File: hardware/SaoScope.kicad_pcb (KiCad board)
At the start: 2 copper layers, 55 x 33 mm, 15 parts, among them J1 Conn_01x03_Pin, J2 Conn_01x04_Socket, SW1 TS-1077S-AR02016, SW2 TS-1077S-AR02016, SW3 TS-1077S-AR02016, SW4 TS-1077S-AR02016, U1 STM32G030F6Px, U2 LMC7660, U3 OPA197xDBV, U4 AP2120N-3.0TRG1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

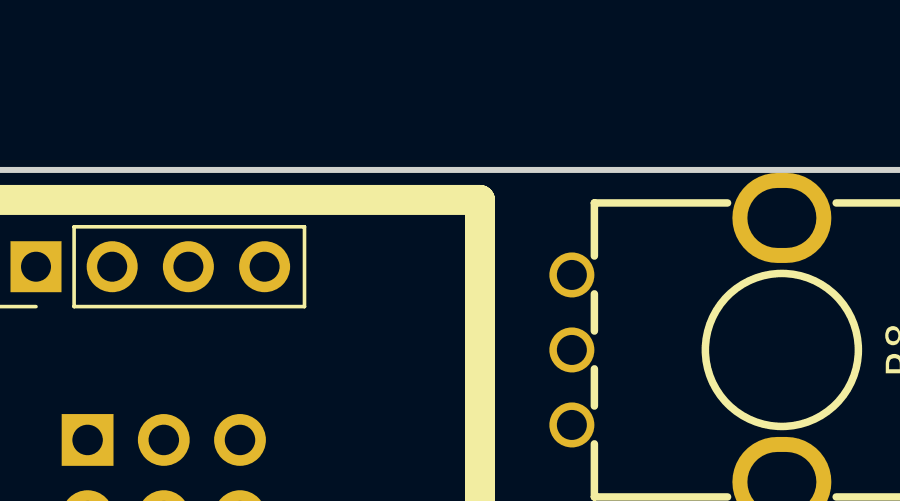
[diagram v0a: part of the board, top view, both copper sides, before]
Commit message: wire up pots and buttons, comments
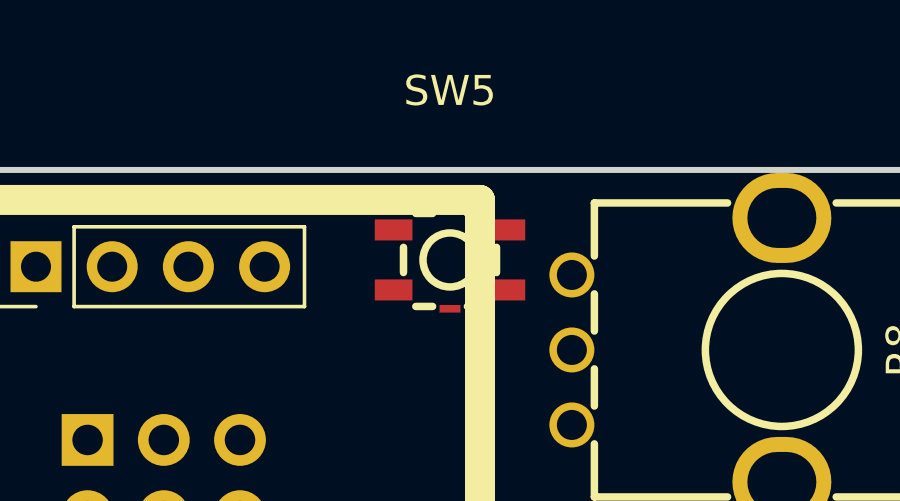
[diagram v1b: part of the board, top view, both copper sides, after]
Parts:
- added SW5: TS-1077S-AR02016, easyeda2kicad:KEY-SMD_4P-L3.1-W3.1-P2.00-LS4.0, F.Cu at (130.0, 64.0)
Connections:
- J2 pad 1: unconnected-(J2-Pin_1-Pad1) -> /I2C_SDA
- J2 pad 2: unconnected-(J2-Pin_2-Pad2) -> /I2C_SCL
- J2 pad 3: unconnected-(J2-Pin_3-Pad3) -> +3.3V
- J2 pad 4: unconnected-(J2-Pin_4-Pad4) -> GND
- R5 pad 1: unconnected-(R5-Pad1) -> Net-(R13-Pad2)
- R5 pad 2: unconnected-(R5-Pad2) -> /DIAL1
- R5 pad 3: unconnected-(R5-Pad3) -> Net-(R5-Pad3)
- R6 pad 1: unconnected-(R6-Pad1) -> Net-(R14-Pad2)
- R6 pad 2: unconnected-(R6-Pad2) -> /DIAL2
- R6 pad 3: unconnected-(R6-Pad3) -> Net-(R10-Pad1)
- R7 pad 1: unconnected-(R7-Pad1) -> Net-(R15-Pad2)
- R7 pad 2: unconnected-(R7-Pad2) -> /DIAL3
- R7 pad 3: unconnected-(R7-Pad3) -> Net-(R11-Pad1)
- R8 pad 1: unconnected-(R8-Pad1) -> Net-(R16-Pad2)
- R8 pad 2: unconnected-(R8-Pad2) -> /DIAL4
- R8 pad 3: unconnected-(R8-Pad3) -> Net-(R12-Pad1)
- SW1 pad 1: unconnected-(SW1-Pad1) -> /DIAL1
- SW1 pad 3: unconnected-(SW1-Pad3) -> GND
- SW1 pad 4: unconnected-(SW1-Pad4) -> GND
- SW2 pad 1: unconnected-(SW2-Pad1) -> /DIAL2
- SW2 pad 3: unconnected-(SW2-Pad3) -> GND
- SW2 pad 4: unconnected-(SW2-Pad4) -> GND
- SW3 pad 1: unconnected-(SW3-Pad1) -> /DIAL3
- SW3 pad 3: unconnected-(SW3-Pad3) -> GND
- SW3 pad 4: unconnected-(SW3-Pad4) -> GND
- SW4 pad 1: unconnected-(SW4-Pad1) -> /DIAL4
- SW4 pad 3: unconnected-(SW4-Pad3) -> GND
- SW4 pad 4: unconnected-(SW4-Pad4) -> GND
- U1 pad 1: unconnected-(U1-PB7/PB8-Pad1) -> /I2C1_SDA
- U1 pad 10: unconnected-(U1-PA3-Pad10) -> /DIAL3
- U1 pad 11: unconnected-(U1-PA4-Pad11) -> /PA4
- U1 pad 12: unconnected-(U1-PA5-Pad12) -> /I2S1_CK
- U1 pad 13: unconnected-(U1-PA6-Pad13) -> /DIAL4
- U1 pad 14: unconnected-(U1-PA7-Pad14) -> /I2S1_SD
- U1 pad 15: unconnected-(U1-PB0/PB1/PB2/PA8-Pad15) -> /I2S1_WS
- U1 pad 16: unconnected-(U1-PA11/PA9-Pad16) -> /PA11/PA9
- U1 pad 17: unconnected-(U1-PA12/PA10-Pad17) -> /PA12/PA10
- U1 pad 18: unconnected-(U1-PA13-Pad18) -> /SYS_SWDIO
- U1 pad 19: unconnected-(U1-PA14/PA15-Pad19) -> /SYS_SWCLK
- U1 pad 2: unconnected-(U1-PC14/PB9-Pad2) -> /RCC_OSC32_IN
- U1 pad 20: unconnected-(U1-PB3/PB4/PB5/PB6-Pad20) -> /I2C_SCL
- U1 pad 3: unconnected-(U1-PC15-Pad3) -> /RCC_OSC32_OUT
- U1 pad 4: unconnected-(U1-VDD-Pad4) -> +3V0
- U1 pad 5: unconnected-(U1-VSS-Pad5) -> GND
- U1 pad 6: unconnected-(U1-NRST-Pad6) -> /NRST
- U1 pad 7: unconnected-(U1-PA0-Pad7) -> /DIAL1
- U1 pad 8: unconnected-(U1-PA1-Pad8) -> /ADC
- U1 pad 9: unconnected-(U1-PA2-Pad9) -> /DIAL2
- X1 pad 1: unconnected-(X1-VCC-Pad1) -> +3.3V
- X1 pad 2: unconnected-(X1-GND-Pad2) -> GND

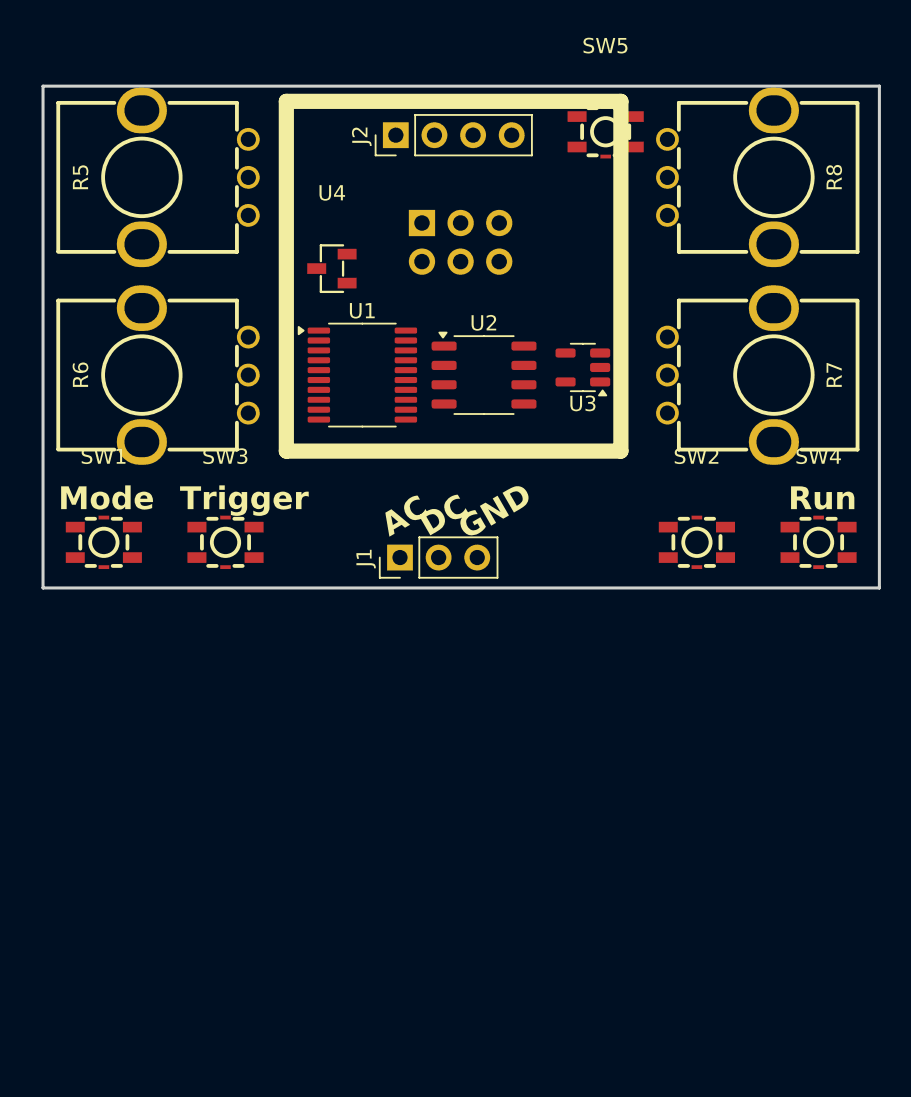
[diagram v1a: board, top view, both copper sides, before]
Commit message: make fit in 50mm
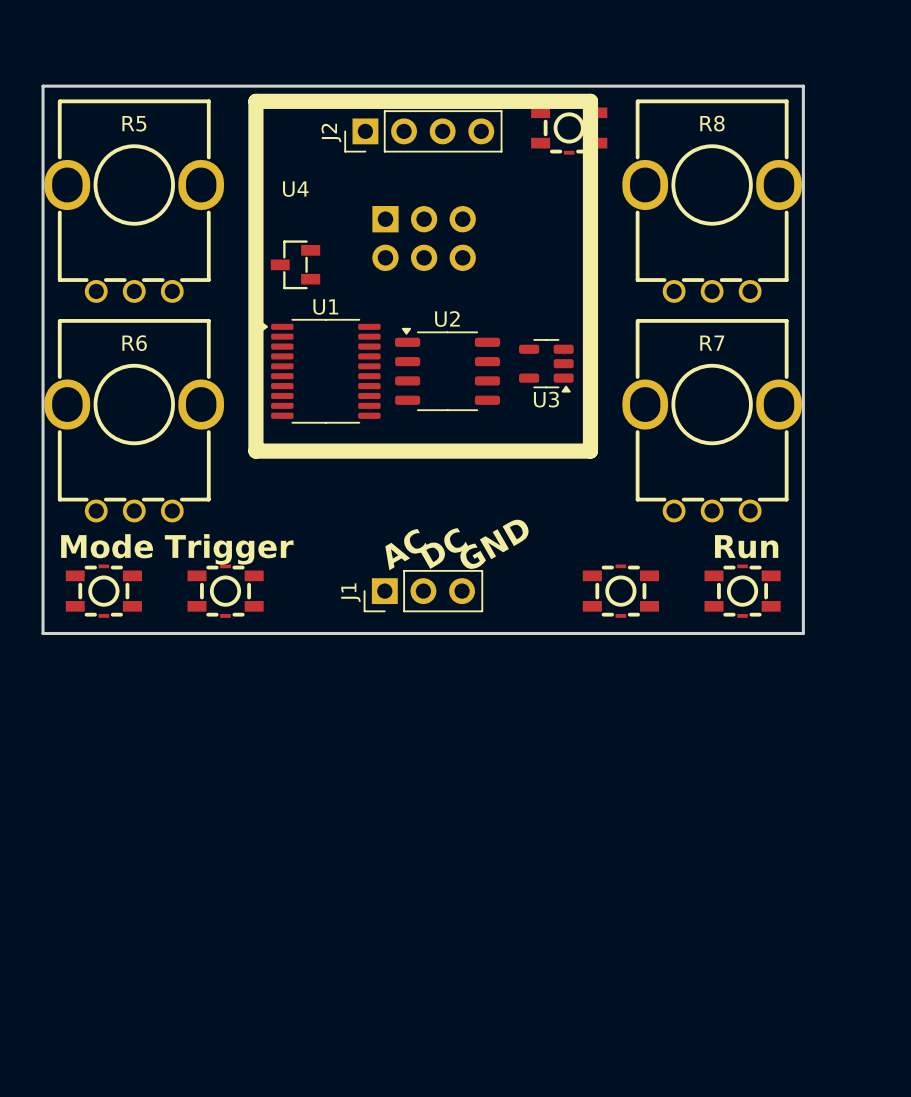
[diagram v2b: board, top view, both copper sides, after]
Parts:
- moved R6 6.75 mm to (99.0, 85.4), turned to 0 degrees
- moved SW2 5.94 mm to (131.0, 94.2)
- moved SW4 5.94 mm to (139.0, 94.2)
- moved R5 5.66 mm to (99.0, 71.0), turned to 0 degrees
- moved R7 5.47 mm to (137.0, 85.4), turned to 0 degrees
- moved R8 4.04 mm to (137.0, 71.0), turned to 0 degrees
- moved SW1 3.21 mm to (97.0, 94.2)
- moved SW3 3.21 mm to (105.0, 94.2)
- moved J1 2.42 mm to (115.5, 94.2)
- moved SW5 2.41 mm to (127.6, 63.8)
- moved U1 2.41 mm to (111.6, 79.8)
- moved U2 2.41 mm to (119.6, 79.8)
- moved U3 2.41 mm to (126.1, 79.2)
- moved U4 2.41 mm to (109.6, 72.8)
- moved X1 2.41 mm to (118.0, 71.0)
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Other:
- board size 55 x 33 mm -> 50 x 36 mm

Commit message: basic rev
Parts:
- added C1: 10uF, Capacitor_SMD:C_0805_2012Metric, F.Cu at (108.0, 73.5)
- added C2: 10uF, Capacitor_SMD:C_0805_2012Metric, F.Cu at (106.0, 77.5)
- added C3: 10uF, Capacitor_SMD:C_0805_2012Metric, F.Cu at (116.0, 79.0)
- added C4: .1uF, Capacitor_SMD:C_0402_1005Metric, F.Cu at (115.5, 89.0)
- added C5: 1uF, Capacitor_SMD:C_0603_1608Metric, F.Cu at (108.0, 68.0)
- added C6: .1uF, Capacitor_SMD:C_0402_1005Metric, F.Cu at (120.0, 82.5)
- added C7: .1uF, Capacitor_SMD:C_0402_1005Metric, F.Cu at (114.0, 82.5)
- added C8: 15pf, Capacitor_SMD:C_0402_1005Metric, F.Cu at (119.5, 76.0)
- added C9: 15pf, Capacitor_SMD:C_0402_1005Metric, F.Cu at (118.8, 81.0)
- added R1: 800K 1%, Resistor_SMD:R_0402_1005Metric, F.Cu at (115.5, 87.5)
- added R2: 200K 1%, Resistor_SMD:R_0402_1005Metric, F.Cu at (113.5, 87.5)
- added R3: 4.7K, Resistor_SMD:R_0402_1005Metric, F.Cu at (117.5, 84.5)
- added R4: 4.7K, Resistor_SMD:R_0402_1005Metric, F.Cu at (117.5, 86.5)
- added RN1: 1K, Resistor_SMD:R_Array_Convex_4x0402, F.Cu at (107.5, 83.0)
- added RN2: 1K, Resistor_SMD:R_Array_Convex_4x0402, F.Cu at (128.5, 75.5)
- added TP1: TestPoint, TestPoint:TestPoint_Pad_1.5x1.5mm, B.Cu at (124.5, 87.6)
- added TP2: TestPoint, TestPoint:TestPoint_Pad_1.5x1.5mm, B.Cu at (124.5, 85.1)
- added TP3: TestPoint, TestPoint:TestPoint_Pad_1.5x1.5mm, B.Cu at (124.5, 82.5)
- added TP4: TestPoint, TestPoint:TestPoint_Pad_1.5x1.5mm, B.Cu at (124.5, 80.0)
- added TP5: TestPoint, TestPoint:TestPoint_Pad_1.5x1.5mm, B.Cu at (124.5, 77.5)
- added Y1: Crystal, Crystal:Crystal_SMD_3215-2Pin_3.2x1.5mm, F.Cu at (119.0, 78.5)
- moved SW3 34.0 mm to (139.0, 94.2)
- moved SW2 26.0 mm to (105.0, 94.2)
- moved U1 13.2 mm to (124.5, 82.5)
- moved U3 12.9 mm to (114.5, 85.0), turned to 0 degrees
- moved U2 8.89 mm to (111.0, 77.5)
- moved SW4 8.00 mm to (131.0, 94.2)
- moved U4 2.76 mm to (108.0, 70.5), turned to -90 degrees
- moved R5 0.50 mm to (99.5, 71.0)
- moved R6 0.50 mm to (99.5, 85.4)
- moved R7 0.50 mm to (136.5, 85.4)
- moved R8 0.50 mm to (136.5, 71.0)
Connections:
- net /I2C_SCL renamed /I2C1_SCL
- J2 pad 1: /I2C_SDA -> /I2C1_SDA
- SW1 pad 2: unconnected-(SW1-Pad2) -> /DIAL1
- SW2 pad 2: unconnected-(SW2-Pad2) -> /DIAL2
- SW3 pad 2: unconnected-(SW3-Pad2) -> /DIAL3
- SW4 pad 2: unconnected-(SW4-Pad2) -> /DIAL4
- SW5 pad 1: unconnected-(SW5-Pad1) -> /SYS_SWCLK
- SW5 pad 4: unconnected-(SW5-Pad4) -> +3V0
- U1 pad 2: /RCC_OSC32_IN -> Net-(U1-PC14/PB9)
- U1 pad 3: /RCC_OSC32_OUT -> Net-(U1-PC15)
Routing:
- net +3V0: track 0.00 -> 75.8 mm, vias 0 -> 2
- net /DIAL1: track 0.00 -> 63.7 mm
- net +3.3V: track 0.00 -> 47.8 mm, vias 0 -> 1
- net GND: track 0.00 -> 47.0 mm, vias 0 -> 31
- net /DIAL2: track 0.00 -> 39.1 mm
- net /DIAL4: track 0.00 -> 37.5 mm, vias 0 -> 2
- net /DIAL3: track 0.00 -> 30.2 mm, vias 0 -> 2
- net /SYS_SWCLK: track 0.00 -> 27.0 mm, vias 0 -> 1
- net /I2C1_SDA: track 0.00 -> 22.5 mm
- net /I2C1_SCL: track 0.00 -> 21.6 mm
- net Net-(RN2B-R2.1): track 0.00 -> 19.8 mm
- net Net-(RN2A-R1.1): track 0.00 -> 17.3 mm
- net Net-(RN1A-R1.1): track 0.00 -> 17.2 mm
- net Net-(RN1B-R2.1): track 0.00 -> 15.6 mm
- net Net-(RN1C-R3.1): track 0.00 -> 13.0 mm
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- added copper zone on B.Cu, net GND
- added copper zone on F.Cu, net GND
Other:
- board text added: "AC/DC"
- board text added: "Edge"
- board text added: "T/Div"
- board text added: "Trg"
- board text added: "V/Div"
- board text added: "VPos"
- board text removed: "Trigger"

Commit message: more graphics/text
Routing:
- net /DIAL4: track 37.5 -> 34.8 mm
- net /DIAL2: track 39.1 -> 40.5 mm
- net Net-(RN2B-R2.1): track 19.8 -> 19.3 mm
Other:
- board size 50 x 36 mm -> 50 x 64 mm
- board text added: "1.75Msps / 500KHz BW"
- board text added: "3.3V"
- board text added: "CLK"
- board text added: "DIO"
- board text added: "NRST"
- board text added: "SaoScope"
- board text added: "V1.0"
- board text added: "± 15V Range"
